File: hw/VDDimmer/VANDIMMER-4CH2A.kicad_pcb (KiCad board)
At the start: 2 copper layers, 100 x 80 mm, 98 parts, among them J1 USB-C 16P, J10 A2 V+SEL VIN/5V, J11 BTN1, J12 BTN2, J13 EXP 3V3/GND/SDA/SCL/EN/IO0, J14 UART1 3V3/GND/TX/RX, J2 VIN 12V, J3 CH1 V+/LED-, J4 CH2 V+/LED-, J5 CH3 V+/LED-, J6 CH4 V+/LED-, J7 ADDR1 V+/D/CLK/GND, J8 ADDR2 V+/D/CLK/GND, J9 A1 V+SEL VIN/5V, Q1 20N06, Q2 20N06, Q3 20N06, Q4 20N06, Q5 SUD50P06-15, U1 ESP32-S3-WROOM-1U-N16, U2 AP63301WU-7, U3 BL1117-33CX, U4 74HCT125, U5 74HCT125

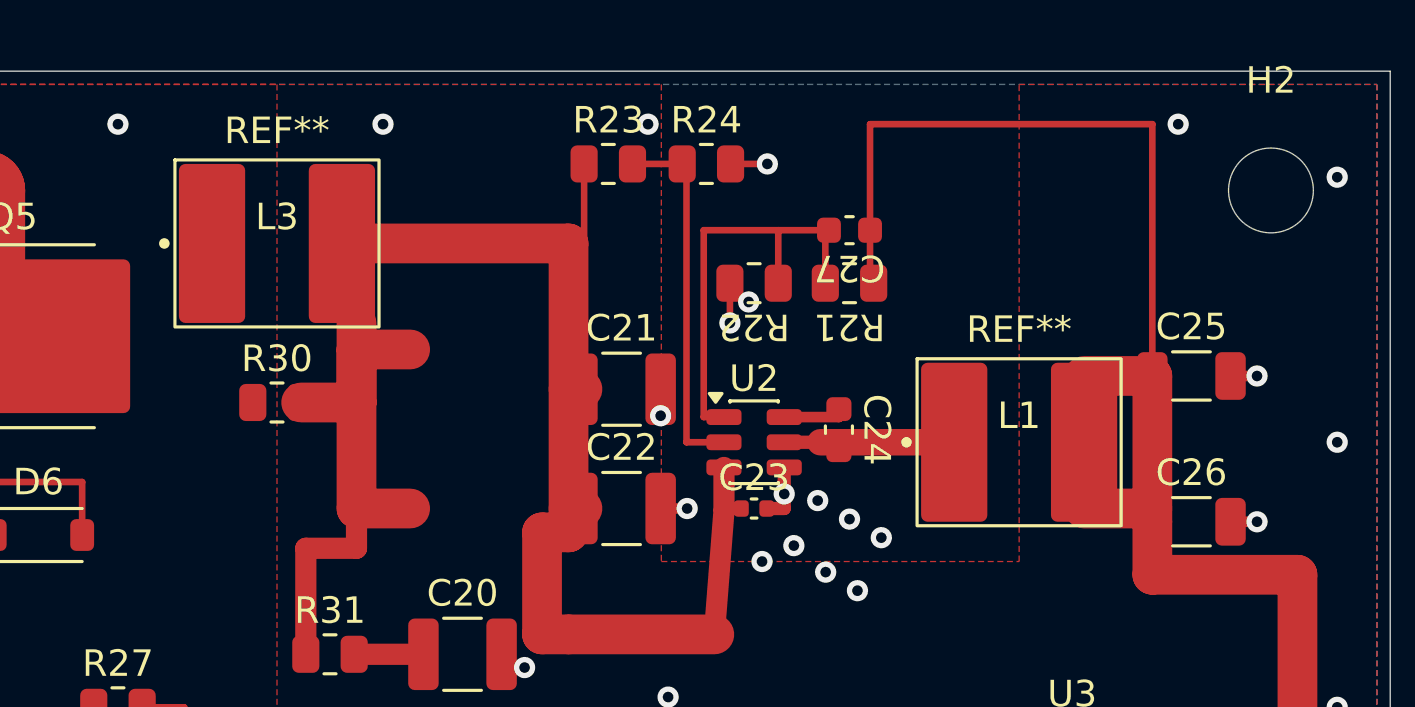
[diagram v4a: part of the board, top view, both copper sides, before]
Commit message: Swap L1/L3 to a curated inductor land, repair routing, clear the courtyard errors
Board side of the change committed at 9b703c8. L1 and L3 now carry
Inductor_SMD:L_Changjiang_FXL0630 (2.35 x 3.50 pads, 6.05 pitch) in place of the
Konnect-generated VANDIMMER footprint whose pads sat 1.15 mm too close together.
R30's (dnp yes) is set, so all three DNPs now report via KiCad's own attribute
rather than a text marker.

Routing repairs
---------------
The old pads were 6.00 mm tall; the new ones are 3.50 mm. Two connections were
caught only by that extra height and broke on the swap:

  L1.2 (+5V)      the two 1.5 mm horizontals end at y=71.5 and y=76.5, outside
                  the new pad's 72.25-75.75 band
  VIN_BUCK        the x=161.0 spine's top end at y=69.5 was bridged by the old
                  L3.2 pad, which reached y=69.5; the new one stops at 68.25

Fixed with two short 1.5 mm tracks, both validated by route.py before pushing.
connect.py then returned to the baseline 12 split nets, with L1.2 back in +5V
group 0 and L3.1 in VIN_PROT group 0 (both via zone fill, which is why a
track-contact check alone still showed them as bare).

Courtyard errors
----------------
The wider land (8.90 mm courtyard vs 7.90) pushed L1's courtyard wings 0.25 mm
into C25 and C26 -- two DRC errors, the first this board has had. Pad clearance
had been checked against every foreign net and was clean; courtyards had not
been. That is the gap.

C25/C26 moved 0.4 mm east rather than moving L1: nothing but board edge lies
east of them, whereas C24's bootstrap cap is 1.25 mm west of L1 and L1 sits in
the switching path. All four moved pads keep their existing track contacts and
conflict with no foreign net. Courtyard gap is now 0.150 mm.

tools/fpspace.py gains --courtyards, a whole-board overlap sweep, negative-tested
against the pre-fix geometry where it reports both overlaps.

Verification
------------
  DRC          0 errors, 166 warnings, 15 unconnected, schematic parity 0
  connect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
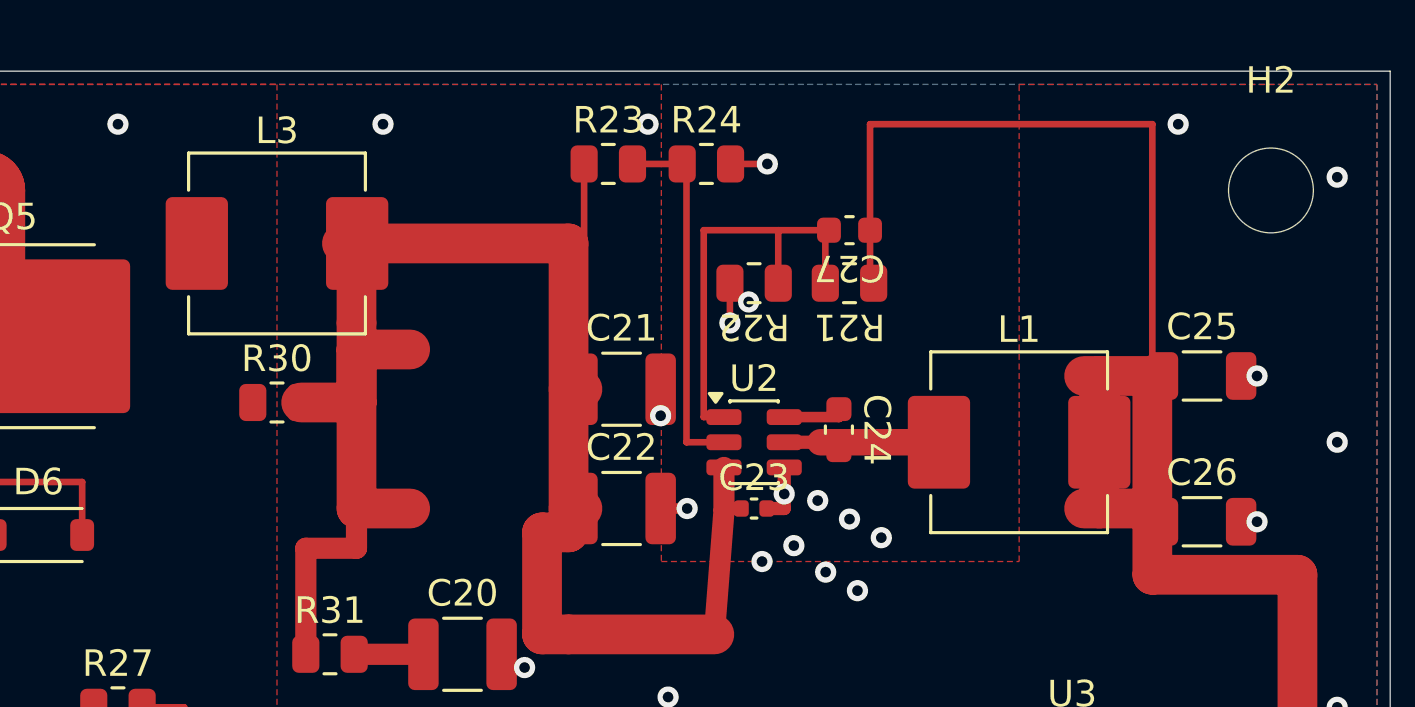
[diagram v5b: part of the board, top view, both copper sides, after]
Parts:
- L1, L3: footprint VANDIMMER:L_cjiang_FXL0630_7.0x6.6mm -> Inductor_SMD:L_Changjiang_FXL0630
- moved C25 0.40 mm to (192.9, 71.5)
- moved C26 0.40 mm to (192.9, 77.0)
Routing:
- net +5V: track 73.1 -> 78.1 mm
- net /Power/VIN_BUCK: track 66.8 -> 69.3 mm

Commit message: Revert the L1/L3 land change: the original geometry was correct
Commits 9b703c8 and 4760f5e moved L1/L3 to KiCad's curated
Inductor_SMD:L_Changjiang_FXL0630 on the reasoning that three independent
curated 6x6 lands agreed with each other and disagreed with the project's
custom footprint. That reasoning was wrong, and installing poppler made it
possible to prove so from the fitted part's own datasheet.

DMBJ PNLS6045, datasheet p3 dimension table: body A=6.0, B=6.0, C(max)=4.50,
terminals D=5.0 x E=1.65 mm. So each terminal spans 1.35-3.00 mm from the
centreline and is 5.0 mm wide.

  land                                pad span    contact       area   of terminal
  L_cjiang_FXL0630_7.0x6.6mm (ours)  1.20-3.70   1.65 x 5.00   8.25    100 %
  Inductor_SMD:L_Changjiang_FXL0630  1.85-4.20   1.15 x 3.50   4.03     49 %

The custom land covers the whole terminal with a 0.70 mm toe. KiCad's covers
half of it and puts 1.20 mm of pad past the body edge. KiCad's land is correct
for an FXL0630 -- a different part -- and must not be used for a PNLS6045.

What went wrong: the footprint is MISNAMED. It is a 6045 land called
L_cjiang_FXL0630_7.0x6.6mm, and it was judged by that name and by comparison
with curated lands for the part the name refers to, without ever checking the
terminal dimensions of the part actually fitted. A curated library land is only
authority for the part it is named after.

The footprint's descr now opens with "MISNAMED - this is a 6045 land, NOT an
FXL0630 7.0x6.6", records the verified terminal geometry, and warns against
substituting KiCad's version. Pads confirmed untouched by that edit. The
filename was left alone deliberately: renaming would mean another schematic
field change, another F8 sync and another round of re-verification, for no
change to the board.

Not reverted, deliberately: C25/C26 stay at x=192.9 (moved 0.4 mm east while the
wider land was fitted). Harmless now the narrower courtyard is back, already
verified there, and moving them again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
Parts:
- L1, L3: footprint Inductor_SMD:L_Changjiang_FXL0630 -> VANDIMMER:L_cjiang_FXL0630_7.0x6.6mm

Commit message: Delete three overlapping drills, restore drill checks to error, clear F1 REF**
The three GND vias whose drills overlapped J1's USB-C shell slots are deleted
(98d41f5d, 0ff36e38, 0ea9cc38). They were redundant: J1.SH is itself a GND
through-hole slot tying both layers, so a stitching via beside it buys nothing --
the same reasoning that retired the via next to J2's PTH GND pad in 0f5083f.

  drill sweep   250 holes, 3 overlapping  ->  247 holes, 0 overlapping
  GND           309 items, 1 connected group, 68 pads -- unchanged
  split nets    12 -- baseline, unchanged

hole_to_hole and holes_co_located are back to `error` severity, and the board
still passes. "0 errors" now carries weight; previously it did not, and that
override hid six drill defects and later three overlapping drills.

F1's stray `REF**` silkscreen text is deleted from the board. The library
footprint still uses legacy fp_text reference/value syntax, so re-importing F1
will reintroduce it -- recorded in HANDOFF, not fixable through MCP.

Also recorded that validate_for_manufacturing reported "READY: 0 issues" while
the board still had three overlapping drills. It checks layer/footprint/net/track
counts only.

Verification
------------
  DRC          0 errors (drill checks at error severity), 165 warnings,
               15 unconnected, schematic parity 0
  drill.py     247 holes, 0 overlapping, 15 pairs below JLC's 0.50 mm standard
  connect.py   12 split nets, GND one group
  courtyards   0 overlaps
  8.5 gate     hot loop 2.51 mm2, B.Cu GND 1 island 7179.8 mm2
  assembly     98 footprints = 77 placed + 18 hand-fit/mechanical + 3 DNP

Renders regenerated.

Co-Authored-By: Claude Opus 5 (1M context) <noreply@anthropic.com>
Claude-Session: https://claude.ai/code/session_01AnYUdWpnpbT2cnPRPqtfVa
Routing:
- net GND: vias 144 -> 141
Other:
- board text added: "VANDIMMER-4CH+2A v 1.0"
- board text removed: "VANDIMMER-4CH+2A"
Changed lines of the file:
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@@
 			(layer "F.Fab")
 		)
-		(fp_text user "REF**"
-			(at 0 -2.7 0)
-			(unlocked yes)
-			(layer "F.SilkS")
-			(effects
-				(font
-					(size 1 1)
-					(thickness 0.15)
-				)
-			)
-		)
 		(fp_text user "Fuse_2410_6125Metric"
 			(at 0 2.7 0)
@@
 		)
 	)
-	(gr_text "VANDIMMER-4CH+2A"
-		(at 166.55 98 0)
+	(gr_text "VANDIMMER-4CH+2A\nv 1.0"
+		(at 113.5 76 0)
 		(layer "F.SilkS")
 		(effects
@@
 	)
 	(via
-		(at 101.962 115.957)
-		(size 0.8)
-		(drill 0.4)
-		(layers "F.Cu" "B.Cu")
-		(net "GND")
-	)
-	(via
-		(at 107.35 116.32)
-		(size 0.8)
-		(drill 0.4)
-		(layers "F.Cu" "B.Cu")
-		(net "GND")
-	)
-	(via
 		(at 114.221 104.95)
 		(size 0.8)
@@
 		(size 0.8)
 		(drill 0.4)
-		(layers "F.Cu" "B.Cu")
-		(net "GND")
-	)
-	(via
-		(at 107.35 107.68)
-		(size 0.8)
-		(drill 0.4)

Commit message: Extend the board to 100x84 so JLCPCB needs no assembly rails
JLC wants >= 5 mm clear of machine-placed copper on two OPPOSITE edges or it adds
rails. Only the south edge qualified. The north edge moved out 4 mm, y 60 -> 56,
so the board is now 100 x 84 mm:

  W   1.80 mm (J1)     under 5
  E   3.45 mm (C63)    under 5
  N   6.80 mm (R23)    OK   -- was 2.80
  S  12.30 mm (PF2)    OK

N and S are now a qualifying pair, so no rails.

Chosen over the alternative of moving R23/R24 2.20 mm and L3 1.50 mm south. That
was verified viable -- pads and courtyards clear, 5 track ends to repair -- but
no case design exists yet, so the outline was still free and growing it touches
no copper at all.

set_board_size could not do this (it appends a second outline; see 9105db3), and
nothing in the toolset deletes a gr_line, so the four y=60 endpoints across three
Edge.Cuts gr_lines were edited directly in the .kicad_pcb. A surgical coordinate
change: no UUIDs, no cross-references, no reordering, against a committed
checkpoint. Note the file is CRLF after a git checkout under core.autocrlf, which
defeated a first attempt matching on "\n".

Verified: 4 Edge.Cuts segments, every corner used exactly twice (closed loop),
extents 100 x 84, and kicad-cli parses it.

Pours deliberately NOT extended into the new strip. They stay inset 0.5 mm from
the old edge, so no existing copper is lost -- B.Cu GND unchanged at 7179.8 mm2
-- and the bare 4 mm does exactly what a rail would have done.

H1/H2 left at y=64.5, now 8.5 mm from the north edge against 4.5 mm elsewhere.
The holes are already verified clear and the case is undrawn, so moving them
buys nothing; the asymmetry is recorded for whoever draws the enclosure.

tools/export-fab.sh replaces the export_manufacturing_package path entirely:
kicad-cli gerbers and drills, our own BOM/CPL, and a self-check that exits
non-zero if the designator sets disagree or any line lacks an LCSC code. It
prints board size and drill counts so a changed outline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
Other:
- board size 100 x 80 mm -> 100 x 84 mm
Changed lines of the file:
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@@
 	)
 	(gr_line
-		(start 100 60)
-		(end 200 60)
+		(start 100 56)
+		(end 200 56)
 		(stroke
 			(width 0.05)
@@
 	(gr_line
 		(start 100 140)
-		(end 100 60)
+		(end 100 56)
 		(stroke
 			(width 0.05)
@@
 	)
 	(gr_line
-		(start 200 60)
+		(start 200 56)
 		(end 200 140)
 		(stroke
